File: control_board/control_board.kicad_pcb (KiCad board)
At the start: 4 copper layers, 93 x 48.1 mm, 49 parts, among them IC1 STM8L151C2T6, J1 ST-LINK Connector, J10 Main_PWR, J11 217182-0001, J12 Mounting_Hole, J13 Mounting_Hole, J14 Mounting_Hole, J2 MCU_HEADER_E, J3 MCU_HEADER_A, J4 Mounting_Hole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

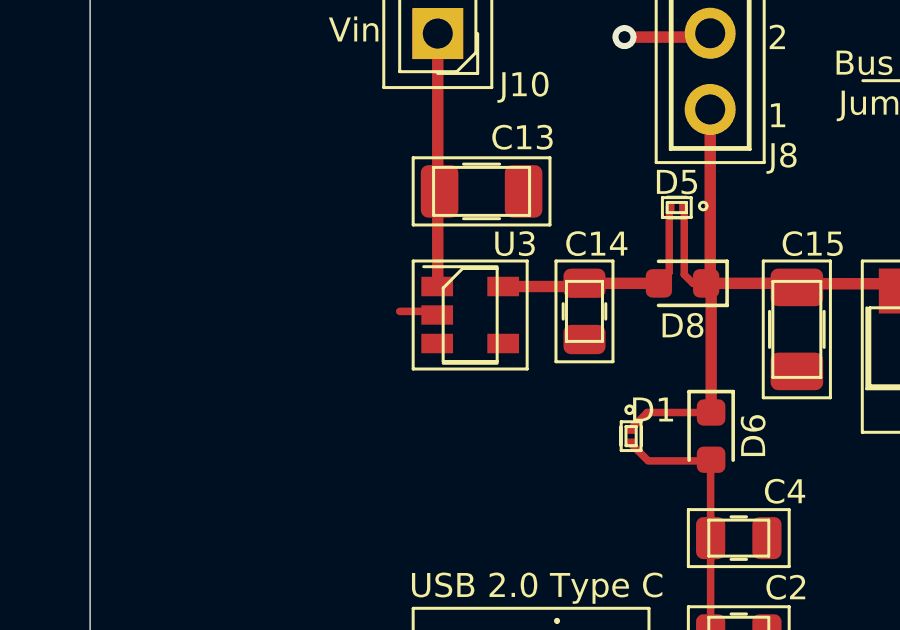
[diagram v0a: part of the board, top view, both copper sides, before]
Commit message: update main regulator input
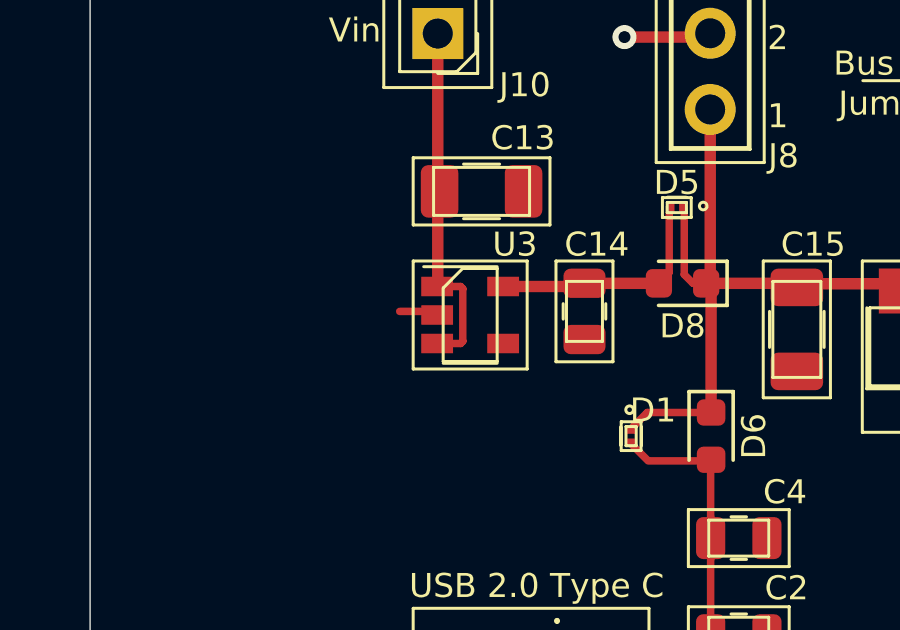
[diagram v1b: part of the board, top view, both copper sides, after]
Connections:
- U3 pad 3: Net-(U3-Pad3) -> VBATT_IN
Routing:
- net VBATT_IN: track 8.20 -> 11.7 mm
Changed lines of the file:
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@@
     (thickness 1.6)
     (drawings 74)
-    (tracks 592)
+    (tracks 597)
     (zones 0)
     (modules 49)
-    (nets 95)
+    (nets 94)
   )
   (page A4)
@@
   (net 79 "Net-(U2-Pad31)")
   (net 80 "Net-(U2-Pad32)")
-  (net 81 "Net-(U3-Pad3)")
-  (net 82 "Net-(U3-Pad4)")
-  (net 83 "Net-(J11-PadB12)")
-  (net 84 "Net-(J11-PadB9)")
-  (net 85 "Net-(J11-PadB8)")
-  (net 86 "Net-(J11-PadB7)")
-  (net 87 "Net-(J11-PadB6)")
-  (net 88 "Net-(J11-PadB5)")
-  (net 89 "Net-(J11-PadB4)")
-  (net 90 "Net-(J11-PadB1)")
-  (net 91 "Net-(J11-PadA12)")
-  (net 92 "Net-(J11-PadA9)")
-  (net 93 "Net-(J11-PadA8)")
-  (net 94 "Net-(J11-PadA5)")
+  (net 81 "Net-(U3-Pad4)")
+  (net 82 "Net-(J11-PadB12)")
+  (net 83 "Net-(J11-PadB9)")
+  (net 84 "Net-(J11-PadB8)")
+  (net 85 "Net-(J11-PadB7)")
+  (net 86 "Net-(J11-PadB6)")
+  (net 87 "Net-(J11-PadB5)")
+  (net 88 "Net-(J11-PadB4)")
+  (net 89 "Net-(J11-PadB1)")
+  (net 90 "Net-(J11-PadA12)")
+  (net 91 "Net-(J11-PadA9)")
+  (net 92 "Net-(J11-PadA8)")
+  (net 93 "Net-(J11-PadA5)")
   (net_class Default "This is the default net class."
     (clearance 0.2)
@@
     (add_net "Net-(U2-Pad8)")
     (add_net "Net-(U2-Pad9)")
-    (add_net "Net-(U3-Pad3)")
     (add_net "Net-(U3-Pad4)")
     (add_net PA4)
@@
       (net 9 "Net-(C14-Pad1)"))
     (pad 4 smd rect (at 1.1 0.95) (size 1.06 0.65) (layers F.Cu F.Paste F.Mask)
-      (net 82 "Net-(U3-Pad4)"))
+      (net 81 "Net-(U3-Pad4)"))
     (pad 3 smd rect (at -1.1 0.95) (size 1.06 0.65) (layers F.Cu F.Paste F.Mask)
-      (net 81 "Net-(U3-Pad3)"))
+      (net 8 VBATT_IN))
     (pad 2 smd rect (at -1.1 0) (size 1.06 0.65) (layers F.Cu F.Paste F.Mask)
       (net 2 GND))
@@
       (net 2 GND))
     (pad 1 smd roundrect (at -1.4 0 90) (size 1.25 1.75) (layers F.Cu F.Paste F.Mask) (roundrect_rratio 0.2)
-      (net 88 "Net-(J11-PadB5)"))
+      (net 87 "Net-(J11-PadB5)"))
     (model ${KISYS3DMOD}/Resistor_SMD.3dshapes/R_1206_3216Metric.wrl
       (at (xyz 0 0 0))
@@
       (net 2 GND))
     (pad 1 smd roundrect (at -1.4 0) (size 1.25 1.75) (layers F.Cu F.Paste F.Mask) (roundrect_rratio 0.2)
-      (net 94 "Net-(J11-PadA5)"))
+      (net 93 "Net-(J11-PadA5)"))
     (model ${KISYS3DMOD}/Resistor_SMD.3dshapes/R_1206_3216Metric.wrl
       (at (xyz 0 0 0))
@@
     (pad MH1 thru_hole circle (at -3.75 0) (size 0.26 0.26) (drill 0.52) (layers *.Cu *.Mask F.SilkS))
     (pad B12 smd rect (at -2.75 0.865 270) (size 0.3 0.87) (layers F.Cu F.Paste F.Mask)
-      (net 83 "Net-(J11-PadB12)"))
+      (net 82 "Net-(J11-PadB12)"))
     (pad B9 smd rect (at -1.25 0.865 270) (size 0.3 0.87) (layers F.Cu F.Paste F.Mask)
-      (net 84 "Net-(J11-PadB9)"))
+      (net 83 "Net-(J11-PadB9)"))
     (pad B8 smd rect (at -0.75 0.865 270) (size 0.3 0.87) (layers F.Cu F.Paste F.Mask)
-      (net 85 "Net-(J11-PadB8)"))
+      (net 84 "Net-(J11-PadB8)"))
     (pad B7 smd rect (at -0.25 0.865 270) (size 0.3 0.87) (layers F.Cu F.Paste F.Mask)
-      (net 86 "Net-(J11-PadB7)"))
+      (net 85 "Net-(J11-PadB7)"))
     (pad B6 smd rect (at 0.25 0.865 270) (size 0.3 0.87) (layers F.Cu F.Paste F.Mask)
-      (net 87 "Net-(J11-PadB6)"))
+      (net 86 "Net-(J11-PadB6)"))
     (pad B5 smd rect (at 0.75 0.865 270) (size 0.3 0.87) (layers F.Cu F.Paste F.Mask)
-      (net 88 "Net-(J11-PadB5)"))
+      (net 87 "Net-(J11-PadB5)"))
     (pad B4 smd rect (at 1.25 0.865 270) (size 0.3 0.87) (layers F.Cu F.Paste F.Mask)
-      (net 89 "Net-(J11-PadB4)"))
+      (net 88 "Net-(J11-PadB4)"))
     (pad B1 smd rect (at 2.75 0.865 270) (size 0.3 0.87) (layers F.Cu F.Paste F.Mask)
-      (net 90 "Net-(J11-PadB1)"))
+      (net 89 "Net-(J11-PadB1)"))
     (pad A12 smd rect (at 2.75 -0.865 270) (size 0.3 0.87) (layers F.Cu F.Paste F.Mask)
-      (net 91 "Net-(J11-PadA12)"))
+      (net 90 "Net-(J11-PadA12)"))
     (pad A9 smd rect (at 1.25 -0.865 270) (size 0.3 0.87) (layers F.Cu F.Paste F.Mask)
-      (net 92 "Net-(J11-PadA9)"))
+      (net 91 "Net-(J11-PadA9)"))
     (pad A8 smd rect (at 0.75 -0.865 270) (size 0.3 0.87) (layers F.Cu F.Paste F.Mask)
-      (net 93 "Net-(J11-PadA8)"))
+      (net 92 "Net-(J11-PadA8)"))
     (pad A7 smd rect (at 0.25 -0.865 270) (size 0.3 0.87) (layers F.Cu F.Paste F.Mask)
       (net 57 USBD-))
@@
       (net 56 USBD+))
     (pad A5 smd rect (at -0.75 -0.865 270) (size 0.3 0.87) (layers F.Cu F.Paste F.Mask)
-      (net 94 "Net-(J11-PadA5)"))
+      (net 93 "Net-(J11-PadA5)"))
     (pad A4 smd rect (at -1.25 -0.865 270) (size 0.3 0.87) (layers F.Cu F.Paste F.Mask)
       (net 3 "Net-(C2-Pad2)"))
@@
   (segment (start 39.14902 35.06702) (end 39.12852 35.08752) (width 0.381) (layer F.Cu) (net 8))
   (segment (start 39.14902 26.89352) (end 39.14902 35.06702) (width 0.381) (layer F.Cu) (net 8))
+  (segment (start 39.90852 35.20752) (end 39.12852 35.20752) (width 0.25) (layer F.Cu) (net 8))
+  (segment (start 39.983521 35.282521) (end 39.90852 35.20752) (width 0.25) (layer F.Cu) (net 8))
+  (segment (start 39.983521 37.032519) (end 39.983521 35.282521) (width 0.25) (layer F.Cu) (net 8))
+  (segment (start 39.90852 37.10752) (end 39.983521 37.032519) (width 0.25) (layer F.Cu) (net 8))
+  (segment (start 39.12852 37.10752) (end 39.90852 37.10752) (width 0.25) (layer F.Cu) (net 8))
   (segment (start 44.04102 35.10252) (end 44.03852 35.10002) (width 0.381) (layer F.Cu) (net 9))
   (segment (start 46.52 35.10252) (end 44.04102 35.10252) (width 0.381) (layer F.Cu) (net 9))
@@
   (segment (start 87.38902 36.92652) (end 87.59952 37.13702) (width 0.25) (layer F.Cu) (net 59))
   (segment (start 83.85152 36.92652) (end 87.38902 36.92652) (width 0.25) (layer F.Cu) (net 59))
-  (segment (start 36.65752 52.15452) (end 36.41852 51.91552) (width 0.25) (layer F.Cu) (net 88))
-  (segment (start 41.58602 52.15452) (end 36.65752 52.15452) (width 0.25) (layer F.Cu) (net 88))
-  (segment (start 48.48052 50.20102) (end 48.03902 50.64252) (width 0.25) (layer F.Cu) (net 94))
-  (segment (start 48.48052 50.00752) (end 48.48052 50.20102) (width 0.25) (layer F.Cu) (net 94))
-  (segment (start 43.31602 50.65452) (end 48.03902 50.64252) (width 0.25) (layer F.Cu) (net 94))
-  (segment (start 48.03902 50.64252) (end 48.04802 50.65452) (width 0.25) (layer F.Cu) (net 94))
+  (segment (start 36.65752 52.15452) (end 36.41852 51.91552) (width 0.25) (layer F.Cu) (net 87))
+  (segment (start 41.58602 52.15452) (end 36.65752 52.15452) (width 0.25) (layer F.Cu) (net 87))
+  (segment (start 48.48052 50.20102) (end 48.03902 50.64252) (width 0.25) (layer F.Cu) (net 93))
+  (segment (start 48.48052 50.00752) (end 48.48052 50.20102) (width 0.25) (layer F.Cu) (net 93))
+  (segment (start 43.31602 50.65452) (end 48.03902 50.64252) (width 0.25) (layer F.Cu) (net 93))
+  (segment (start 48.03902 50.64252) (end 48.04802 50.65452) (width 0.25) (layer F.Cu) (net 93))
   (zone (net 2) (net_name GND) (layer F.Cu) (hatch edge 0.508)
     (connect_pads (clearance 0.508))
